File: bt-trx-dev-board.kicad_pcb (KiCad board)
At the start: 2 copper layers, 78 x 68 mm, 59 parts, among them J1 RJ45, J10 Conn_01x08, J11 VOX_IN, J12 VOX_TRX, J2 PTT_BUTTON, J3 PTT_CON, J5 PTT_SEL, J6 I2C, J7 Conn_01x02, J8 I2C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

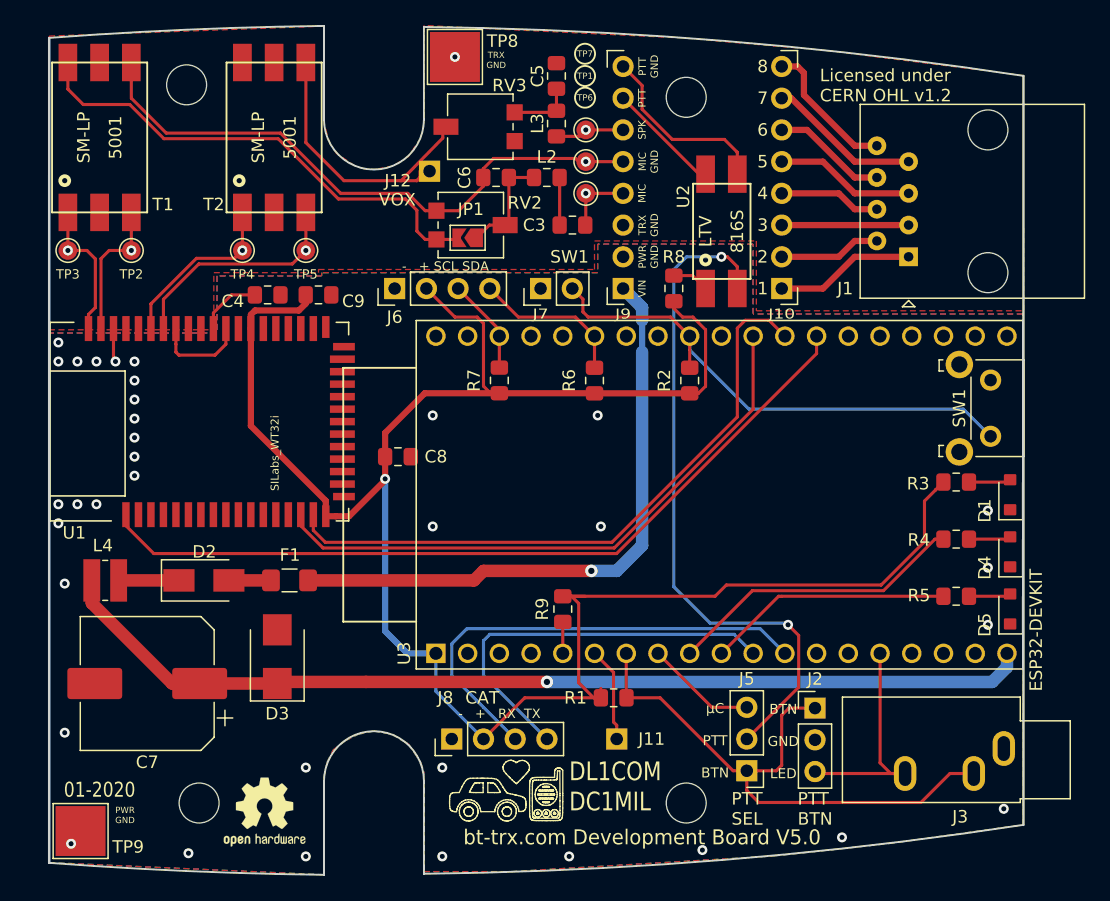
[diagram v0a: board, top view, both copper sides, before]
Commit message: anm: Added FMB100 to PCB
* Replaced WT32i with FMB100
* Swapped RX and TX transformers
* Removed MIC Bias C
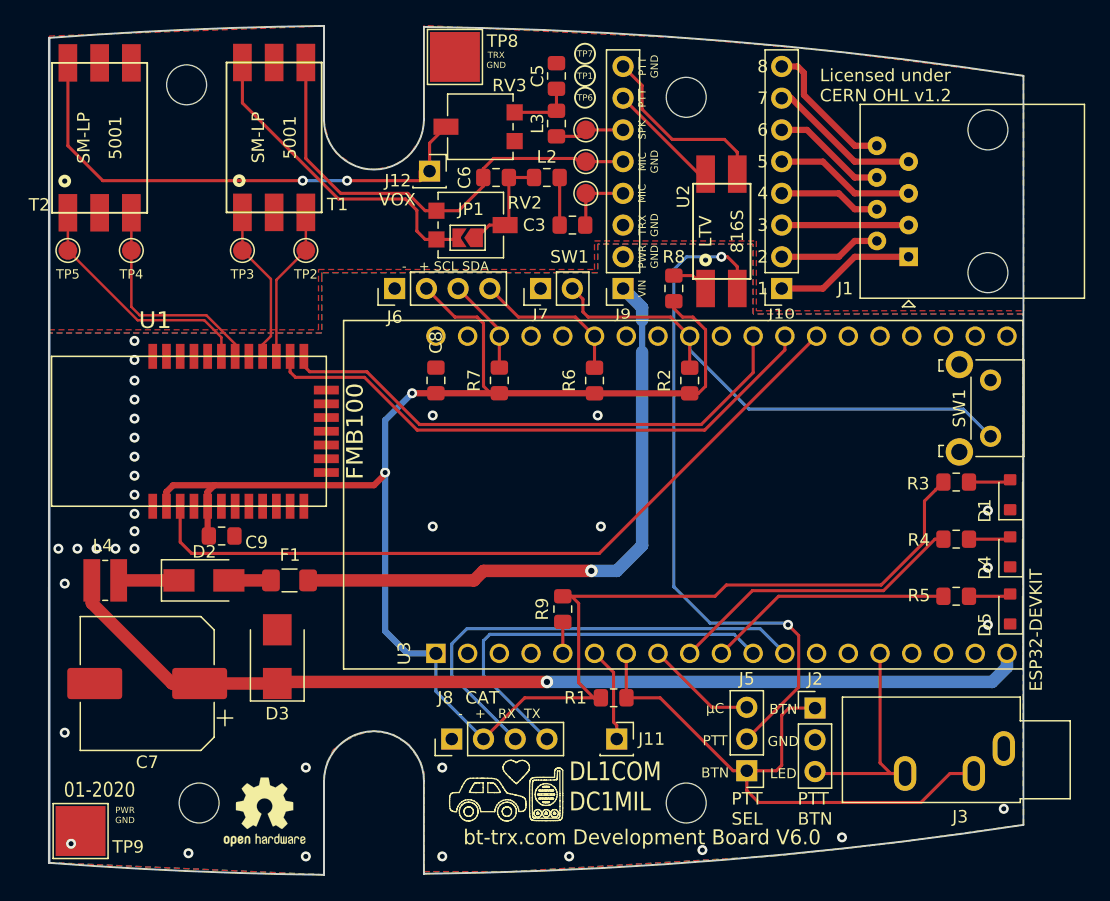
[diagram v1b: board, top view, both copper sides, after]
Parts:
- removed C4: 1uF, Capacitor_SMD:C_0805_2012Metric_Pad1.15x1.40mm_HandSolder
- J10: value Conn_01x08 -> JMP_CON_TRX
- J7: value Conn_01x02 -> SW1_CON
- J9: value Conn_01x08 -> JMP_CON
- U1: value SILabs_WT32i -> FMB100; footprint wt32i:LGA50-1.0-23.9X15.9MM -> FMB100:FMB100
- moved C9 20.8 mm to (134.2, 106.2)
- moved TP5 19.0 mm to (121.9, 83.3)
- moved T2 14.0 mm to (121.9, 80.3)
- moved TP2 14.0 mm to (141.0, 83.3)
- moved T1 14.0 mm to (135.9, 80.3)
- moved TP3 14.0 mm to (135.9, 83.3)
- moved TP4 8.89 mm to (127.0, 83.3)
- moved C8 6.82 mm to (151.4, 93.7), turned to -90 degrees
- moved U1 2.14 mm to (142.6, 103.8), turned to 0 degrees
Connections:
- T2 pad 1: /A_IN_LN -> /A_IN_LP
- T2 pad 3: /A_IN_LP -> /A_IN_LN
- T2 pad 4: /VOX -> GND
- T2 pad 6: GND -> /VOX
- U1 pad 1: /WT32_ONOFF_FROM_UC -> GNDPWR
- U1 pad 10: (no net) -> unconnected-(U1-Pad10)
- U1 pad 11: (no net) -> unconnected-(U1-Pad11)
- U1 pad 12: (no net) -> unconnected-(U1-Pad12)
- U1 pad 13: (no net) -> unconnected-(U1-Pad13)
- U1 pad 14: (no net) -> unconnected-(U1-Pad14)
- U1 pad 15: /UART_UC_TX -> unconnected-(U1-Pad15)
- U1 pad 16: /UART_UC_RX -> unconnected-(U1-Pad16)
- U1 pad 17: +3V3 -> unconnected-(U1-Pad17)
- U1 pad 18: GNDPWR -> unconnected-(U1-Pad18)
- U1 pad 19: (no net) -> unconnected-(U1-Pad19)
- U1 pad 2: GNDPWR -> +3V3
- U1 pad 20: (no net) -> /UART_UC_TX
- U1 pad 21: (no net) -> /UART_UC_RX
- U1 pad 22: (no net) -> /A_OUT_LN
- U1 pad 23: (no net) -> /A_OUT_LP
- U1 pad 24: (no net) -> unconnected-(U1-Pad24)
- U1 pad 25: (no net) -> /A_IN_LN
- U1 pad 26: (no net) -> /A_IN_LP
- U1 pad 27: (no net) -> unconnected-(U1-Pad27)
- U1 pad 28: (no net) -> unconnected-(U1-Pad28)
- U1 pad 29: (no net) -> GNDPWR
- U1 pad 3: GNDPWR -> /WT32_ONOFF_FROM_UC
- U1 pad 30: (no net) -> GNDPWR
- U1 pad 4: GNDPWR -> unconnected-(U1-Pad4)
- U1 pad 5: (no net) -> +3V3
- U1 pad 6: (no net) -> unconnected-(U1-Pad6)
- U1 pad 7: (no net) -> GNDPWR
- U1 pad 8: (no net) -> unconnected-(U1-Pad8)
- U1 pad 9: (no net) -> unconnected-(U1-Pad9)
- U3 pad 13: (no net) -> unconnected-(U3-Pad13)
- U3 pad 16: (no net) -> unconnected-(U3-Pad16)
- U3 pad 17: (no net) -> unconnected-(U3-Pad17)
- U3 pad 18: (no net) -> unconnected-(U3-Pad18)
- U3 pad 2: (no net) -> unconnected-(U3-Pad2)
- U3 pad 21: (no net) -> unconnected-(U3-Pad21)
- U3 pad 23: (no net) -> unconnected-(U3-Pad23)
- U3 pad 24: (no net) -> unconnected-(U3-Pad24)
- U3 pad 27: (no net) -> unconnected-(U3-Pad27)
- U3 pad 29: (no net) -> unconnected-(U3-Pad29)
- U3 pad 3: (no net) -> unconnected-(U3-Pad3)
- U3 pad 33: (no net) -> unconnected-(U3-Pad33)
- U3 pad 34: (no net) -> unconnected-(U3-Pad34)
- U3 pad 35: (no net) -> unconnected-(U3-Pad35)
- U3 pad 36: (no net) -> unconnected-(U3-Pad36)
- U3 pad 37: (no net) -> unconnected-(U3-Pad37)
- U3 pad 38: (no net) -> unconnected-(U3-Pad38)
- U3 pad 4: (no net) -> unconnected-(U3-Pad4)
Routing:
- net /VOX: track 24.5 -> 41.7 mm, vias 0 -> 2
- net Net-(JP1-Pad2): track 39.0 -> 26.9 mm
- net GNDA: track 48.2 -> 37.5 mm, vias 1 -> 0
- net GNDPWR: track 10.3 -> 0.00 mm
- net +3V3: track 167.4 -> 158.3 mm, vias 1 -> 2
- net Net-(C4-Pad2): track 5.17 -> 0.00 mm
- net /UART_UC_TX: track 48.3 -> 43.3 mm
- net /UART_UC_RX: track 51.5 -> 46.6 mm
- net /WT32_ONOFF_FROM_UC: track 65.1 -> 61.4 mm
- net /A_IN_LN: track 15.0 -> 18.1 mm, vias 1 -> 0
- net /A_OUT_LP: track 11.3 -> 12.7 mm, vias 1 -> 0
- net /A_OUT_LN: track 11.3 -> 12.5 mm, vias 1 -> 0
- net GND: track 0.75 -> 0.00 mm, vias 1 -> 0
- net /A_IN_LP: track 19.3 -> 19.7 mm, vias 1 -> 0
- net /AUDIO_OUT_MIC: vias 1 -> 0
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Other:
- net class Default removed
- net class Thick removed
- board text added: "bt-trx.com Development Board V6.0"
- board text removed: "bt-trx.com Development Board V5.0"

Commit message: am: fixed #30 Suboptimal placement of D3
* Swapped D3 and L4 according to Issue #30
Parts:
- moved D3 2.07 mm to (139.1, 113.8), turned to 0 degrees
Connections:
- D3 pad 1: +5V -> Net-(D2-Pad1)
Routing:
- net Net-(D2-Pad1): track 4.83 -> 12.6 mm
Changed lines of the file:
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@@
   )
   (footprint "Diode_SMD:D_SMB" (layer "F.Cu")
-    (at 138.684 115.833 90)
+    (at 139.056 113.792)
     (descr "Diode SMB (DO-214AA)")
     (tags "Diode SMB (DO-214AA)")
@@
     (property "Sheetname" "Microcontroller")
     (attr smd)
-    (fp_text reference "D3" (at -4.563 0) (layer "F.SilkS")
+    (fp_text reference "D3" (at -4.563 0 90) (layer "F.SilkS")
       (effects (font (size 1 1) (thickness 0.15)))
     )
-    (fp_text value "TVS 16V" (at 0 3.1 270) (layer "F.Fab")
+    (fp_text value "TVS 16V" (at 0 3.1) (layer "F.Fab")
       (effects (font (size 1 1) (thickness 0.15)))
     )
-    (fp_text user "${REFERENCE}" (at 0 -3 270) (layer "F.Fab")
+    (fp_text user "${REFERENCE}" (at 0 -3) (layer "F.Fab")
       (effects (font (size 1 1) (thickness 0.15)))
     )
@@
     (fp_line (start -0.64944 -0.79908) (end -0.64944 0.80112) (layer "F.Fab") (width 0.1))
     (fp_line (start -2.3 2) (end -2.3 -2) (layer "F.Fab") (width 0.1))
-    (pad "1" smd rect (at -2.15 0 90) (size 2.5 2.3) (layers "F.Cu" "F.Paste" "F.Mask")
-      (net 3 "+5V") (pinfunction "K") (pintype "passive"))
-    (pad "2" smd rect (at 2.15 0 90) (size 2.5 2.3) (layers "F.Cu" "F.Paste" "F.Mask")
+    (pad "1" smd rect (at -2.15 0) (size 2.5 2.3) (layers "F.Cu" "F.Paste" "F.Mask")
+      (net 12 "Net-(D2-Pad1)") (pinfunction "K") (pintype "passive"))
+    (pad "2" smd rect (at 2.15 0) (size 2.5 2.3) (layers "F.Cu" "F.Paste" "F.Mask")
       (net 28 "GNDPWR") (pinfunction "A") (pintype "passive"))
     (model "${KICAD6_3DMODEL_DIR}/Diode_SMD.3dshapes/D_SMB.wrl"
@@
   (segment (start 151.384 118.618) (end 155.194 122.428) (width 0.25) (layer "B.Cu") (net 2))
   (segment (start 147.32 113.792) (end 149.098 115.57) (width 0.5) (layer "B.Cu") (net 2))
-  (segment (start 132.47 117.983) (end 138.684 117.983) (width 1) (layer "F.Cu") (net 3))
+  (segment (start 132.597 117.856) (end 132.47 117.983) (width 1) (layer "F.Cu") (net 3))
   (segment (start 123.834 109.728) (end 123.834 111.547) (width 1) (layer "F.Cu") (net 3))
   (segment (start 130.27 117.983) (end 132.47 117.983) (width 1) (layer "F.Cu") (net 3))
-  (segment (start 138.811 117.856) (end 160.274 117.856) (width 1) (layer "F.Cu") (net 3))
+  (segment (start 160.274 117.856) (end 132.597 117.856) (width 1) (layer "F.Cu") (net 3))
   (segment (start 123.834 111.547) (end 130.27 117.983) (width 1) (layer "F.Cu") (net 3))
-  (segment (start 138.811 117.856) (end 138.684 117.983) (width 1) (layer "F.Cu") (net 3))
   (via (at 160.274 117.856) (size 1) (drill 0.5) (layers "F.Cu" "B.Cu") (net 3))
   (segment (start 197.104 115.57) (end 197.104 116.673086) (width 1) (layer "B.Cu") (net 3))
@@
   (segment (start 178.816 110.998) (end 192.015 110.998) (width 0.25) (layer "F.Cu") (net 11))
   (segment (start 130.81 109.728) (end 125.984 109.728) (width 1) (layer "F.Cu") (net 12))
+  (segment (start 130.81 109.728) (end 134.874 113.792) (width 1) (layer "F.Cu") (net 12))
+  (segment (start 134.874 113.792) (end 136.906 113.792) (width 1) (layer "F.Cu") (net 12))
   (segment (start 197.174 110.998) (end 197.358 110.814) (width 0.25) (layer "F.Cu") (net 13))
   (segment (start 194.065 110.998) (end 197.174 110.998) (width 0.25) (layer "F.Cu") (net 13))
@@
         (xy 142.24 85.09)
         (xy 142.24 85.344)
-        (xy 142.24 85.344)
         (xy 142.24 89.916)
         (xy 120.396 89.916)
@@
         (xy 141.986 89.662)
         (xy 141.986 85.09)
-        (xy 141.986 85.09)
         (xy 141.986 84.836)
         (xy 164.084 84.836)
@@
         (xy 142.24 85.09)
         (xy 142.24 85.344)
-        (xy 142.24 85.344)
         (xy 142.24 89.916)

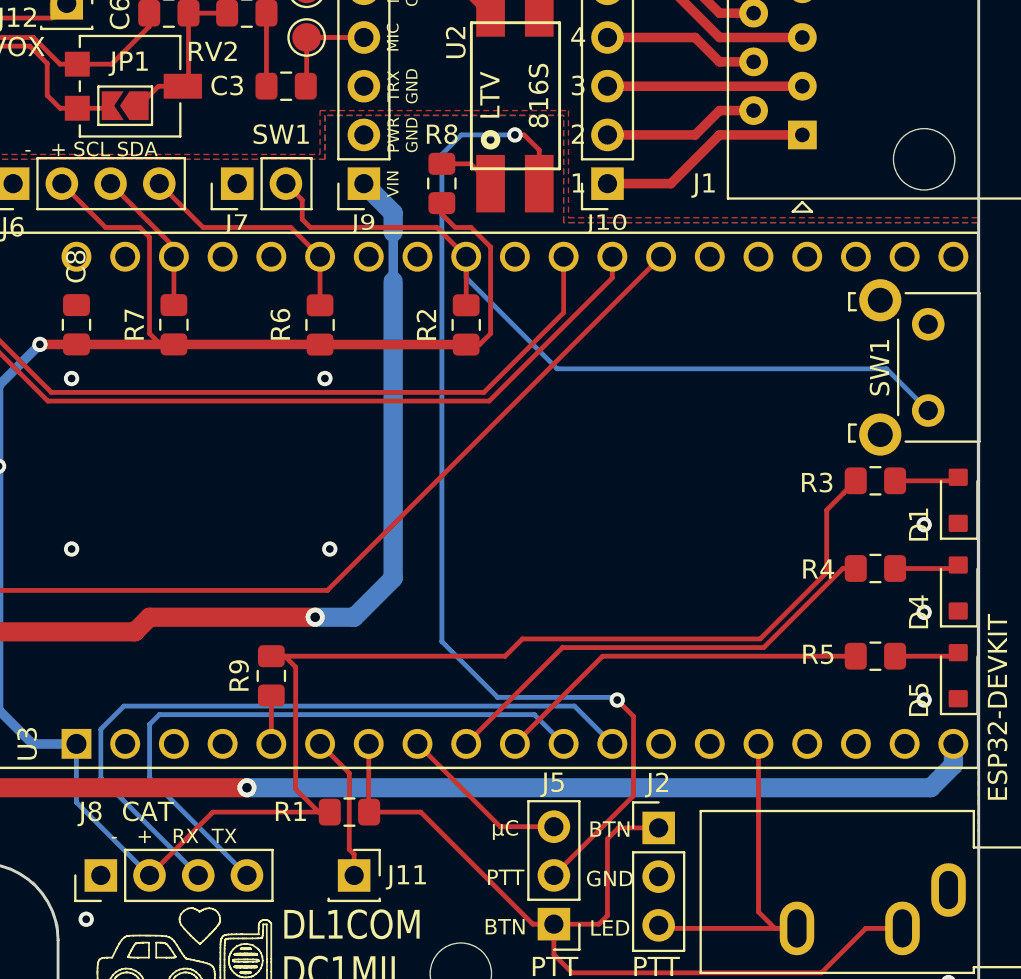
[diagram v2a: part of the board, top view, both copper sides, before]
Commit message: am: Modified HW indication voltage
* Added R10 for voltage divider (v6.x == 1.65V)
* Replaced all R footprints with current ones from KiCad lib
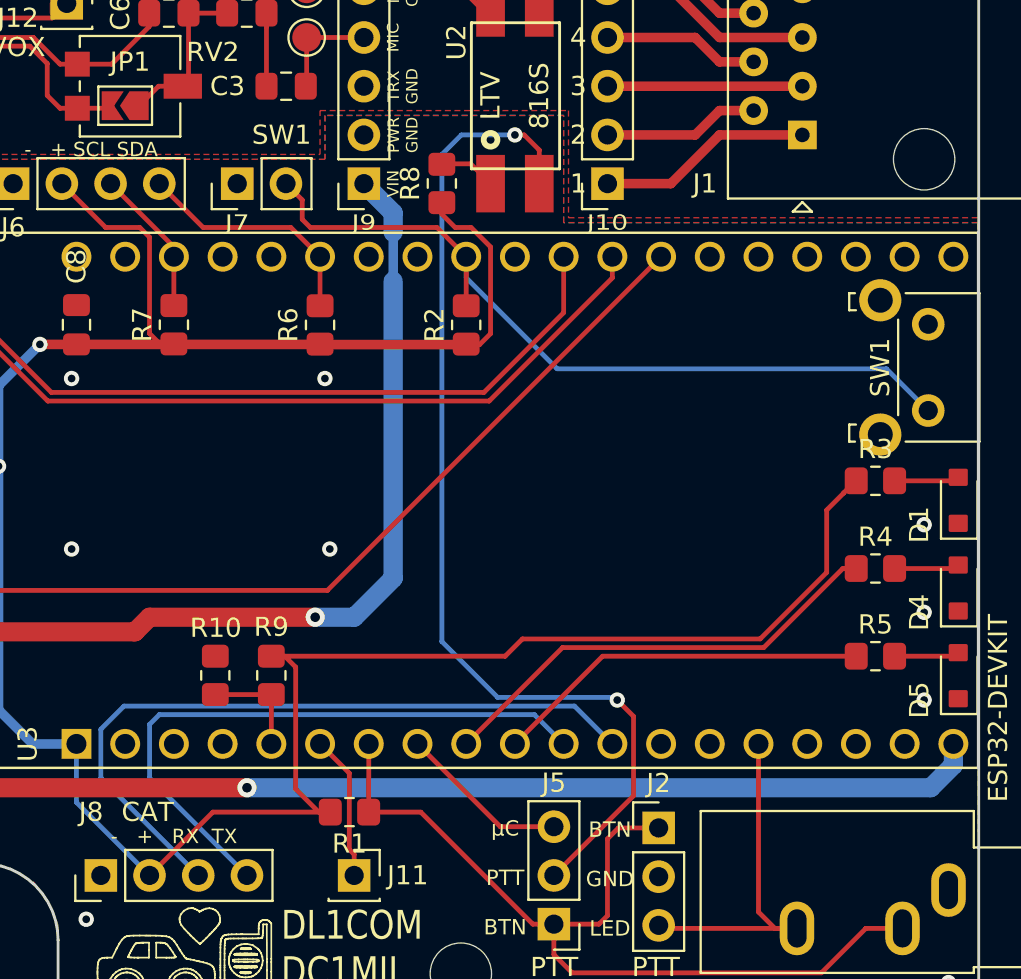
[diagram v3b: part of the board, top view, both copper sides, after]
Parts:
- added R10: 10k, Resistor_SMD:R_0805_2012Metric_Pad1.20x1.40mm_HandSolder, F.Cu at (158.6, 112.0)
- R1, R2, R3, R4, R5, R6, R7, R8, R9: footprint Resistor_SMD:R_0805_2012Metric_Pad1.15x1.40mm_HandSolder -> Resistor_SMD:R_0805_2012Metric_Pad1.20x1.40mm_HandSolder
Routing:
- net /Microcontroller/HW_VER: track 2.52 -> 5.49 mm
